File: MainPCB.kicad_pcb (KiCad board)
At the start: 4 copper layers, 105 x 62.4 mm, 42 parts, among them J1 RaspberryPi, J10 Conn_01x02, J12 Conn_01x07, J2 Conn_01x03, J3 Screw_Terminal_01x02, J4 Conn_01x02, J5 Conn_01x06, J6 Conn_01x03_Pin, J8 Conn_01x12, J9 Conn_01x04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

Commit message: Fixed Regulator Pins
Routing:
- net GND: track 398.8 -> 401.2 mm
- net 12V: track 240.5 -> 242.6 mm
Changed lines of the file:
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@@
 			)
 		)
+		(property ki_fp_filters "Connector*:*_1x??_*")
+		(sheetname "Root")
+		(sheetfile "MainPCB.kicad_sch")
 		(attr through_hole)
 		(fp_line
@@
 			(remove_unused_layers no)
 			(net 1 "GND")
-			(pinfunction "IN-")
+			(pinfunction "OUT-")
 			(pintype "input")
 		)
@@
 			)
 		)
+		(property ki_fp_filters "Connector*:*_1x??_*")
+		(sheetname "Root")
+		(sheetfile "MainPCB.kicad_sch")
 		(attr through_hole)
 		(fp_line
@@
 			)
 		)
-		(sheetname "Root")
-		(sheetfile "MainPCB.kicad_sch")
 		(attr through_hole)
 		(fp_rect
@@
 		)
 		(pad "1" thru_hole circle
-			(at 16.53 -1.27)
+			(at 6.37 -1.27)
 			(size 1.524 1.524)
 			(drill 0.762)
 			(layers "*.Cu" "*.Mask")
 			(remove_unused_layers no)
+			(pinfunction "OUT+")
+			(pintype "input")
 		)
 		(pad "3" thru_hole circle
-			(at 13.99 -1.27)
+			(at 8.91 -1.27)
 			(size 1.524 1.524)
 			(drill 0.762)
@@
 		)
 		(pad "4" thru_hole circle
-			(at 8.91 -1.27)
+			(at 11.45 -1.27)
 			(size 1.524 1.524)
 			(drill 0.762)
@@
 			(remove_unused_layers no)
 			(net 1 "GND")
-			(pinfunction "OUT-")
+			(pinfunction "IN-")
 			(pintype "input")
 		)
 		(pad "4" thru_hole circle
-			(at 11.45 -1.27)
+			(at 13.99 -1.27)
 			(size 1.524 1.524)
 			(drill 0.762)
@@
 			(remove_unused_layers no)
 			(net 1 "GND")
-			(pinfunction "OUT-")
+			(pinfunction "IN-")
 			(pintype "input")
 		)
 		(pad "5" thru_hole circle
-			(at 6.37 -1.27)
+			(at 16.53 -1.27)
 			(size 1.524 1.524)
 			(drill 0.762)
@@
 	)
 	(segment
-		(start 135.01 123.96)
-		(end 137.55 123.96)
-		(width 0.25)
+		(start 125.12 86.2)
+		(end 130.72 80.6)
+		(width 0.3)
 		(layer "F.Cu")
 		(net 1)
 	)
 	(segment
-		(start 125.12 86.2)
-		(end 130.72 80.6)
+		(start 137.55 123.96)
+		(end 140.09 123.96)
 		(width 0.3)
 		(layer "F.Cu")
@@
 	)
 	(segment
+		(start 120.6927 125.1439)
+		(end 113.9324 118.3836)
+		(width 0.3)
+		(layer "In1.Cu")
+		(net 1)
+	)
+	(segment
 		(start 177.8 120.2181)
 		(end 177.8 117.6)
@@
 	)
 	(segment
+		(start 136.3661 125.1439)
+		(end 120.6927 125.1439)
+		(width 0.3)
+		(layer "In1.Cu")
+		(net 1)
+	)
+	(segment
 		(start 162.8 81.3)
 		(end 166.9 85.4)
@@
 	)
 	(segment
+		(start 137.55 123.96)
+		(end 136.3661 125.1439)
+		(width 0.3)
+		(layer "In1.Cu")
+		(net 1)
+	)
+	(segment
 		(start 150.4261 97.0839)
 		(end 150.4261 111.3061)
@@
 	)
 	(segment
-		(start 134.0061 125.1439)
-		(end 120.6927 125.1439)
-		(width 0.3)
-		(layer "In1.Cu")
-		(net 1)
-	)
-	(segment
 		(start 137.578 79.3992)
 		(end 137.578 71.4128)
@@
 	)
 	(segment
-		(start 135.12 124.03)
-		(end 134.0061 125.1439)
-		(width 0.3)
-		(layer "In1.Cu")
-		(net 1)
-	)
-	(segment
 		(start 174.82 123.1981)
 		(end 177.8 120.2181)
@@
 	)
 	(segment
-		(start 120.6927 125.1439)
-		(end 113.9324 118.3836)
-		(width 0.3)
-		(layer "In1.Cu")
-		(net 1)
-	)
-	(segment
 		(start 113.27 111.2451)
 		(end 114.92 112.8951)
@@
 	)
 	(segment
-		(start 114.887968 109.14)
-		(end 114.54 109.14)
-		(width 1)
+		(start 146.03 120.56)
+		(end 151.307767 120.56)
+		(width 0.4)
 		(layer "F.Cu")
 		(net 3)
@@
 	)
 	(segment
-		(start 132.47 123.96)
-		(end 135.87 120.56)
-		(width 0.4)
+		(start 142.63 123.96)
+		(end 139.18 120.51)
+		(width 1)
 		(layer "F.Cu")
 		(net 3)
 	)
 	(segment
-		(start 157.15 112.91)
-		(end 158.4 111.66)
+		(start 157.15 114.717767)
+		(end 157.15 112.91)
 		(width 0.4)
 		(layer "F.Cu")
@@
 	)
 	(segment
-		(start 132.47 123.96)
-		(end 129.02 120.51)
+		(start 126.257968 120.51)
+		(end 114.887968 109.14)
+		(width 1)
+		(layer "F.Cu")
+		(net 3)
+	)
+	(segment
+		(start 114.887968 109.14)
+		(end 114.54 109.14)
 		(width 1)
 		(layer "F.Cu")
@@
 	)
 	(segment
-		(start 135.87 120.56)
-		(end 151.307767 120.56)
+		(start 157.15 112.91)
+		(end 158.4 111.66)
 		(width 0.4)
 		(layer "F.Cu")
@@
 	)
 	(segment
-		(start 157.15 114.717767)
-		(end 157.15 112.91)
+		(start 151.307767 120.56)
+		(end 157.15 114.717767)
 		(width 0.4)
 		(layer "F.Cu")
@@
 	)
 	(segment
-		(start 151.307767 120.56)
-		(end 157.15 114.717767)
+		(start 142.63 123.96)
+		(end 146.03 120.56)
 		(width 0.4)
 		(layer "F.Cu")
@@
 	)
 	(segment
-		(start 129.02 120.51)
+		(start 139.18 120.51)
 		(end 126.257968 120.51)
 		(width 1)
@@
 	)
 	(segment
-		(start 126.257968 120.51)
-		(end 114.887968 109.14)
-		(width 1)
-		(layer "F.Cu")
-		(net 3)
-	)
-	(segment
 		(start 89.56 86.2)
 		(end 95.84 92.48)
@@
 	)
 	(segment
-		(start 171.6592 109.5092)
-		(end 146.8384 109.5092)
+		(start 175.3 116.7303)
+		(end 174.05 115.4803)
 		(width 2)
 		(layer "In2.Cu")
@@
 	)
 	(segment
-		(start 146.8384 109.5092)
-		(end 140.09 116.2576)
+		(start 135.01 121.3376)
+		(end 135.01 123.96)
 		(width 2)
 		(layer "In2.Cu")
@@
 	)
 	(segment
-		(start 174.05 111.9)
-		(end 171.6592 109.5092)
+		(start 174.05 115.4803)
+		(end 174.05 111.9)
 		(width 2)
 		(layer "In2.Cu")
@@
 	)
 	(segment
-		(start 175.3 116.7303)
-		(end 174.05 115.4803)
+		(start 171.6592 109.5092)
+		(end 146.8384 109.5092)
 		(width 2)
 		(layer "In2.Cu")
@@
 	)
 	(segment
-		(start 175.3 117.6)
-		(end 175.3 116.7303)
+		(start 146.8384 109.5092)
+		(end 135.01 121.3376)
 		(width 2)
 		(layer "In2.Cu")
@@
 	)
 	(segment
-		(start 174.05 115.4803)
-		(end 174.05 111.9)
+		(start 175.3 117.6)
+		(end 175.3 116.7303)
 		(width 2)
 		(layer "In2.Cu")
@@
 	)
 	(segment
-		(start 140.09 116.2576)
-		(end 140.09 123.96)
+		(start 174.05 111.9)
+		(end 171.6592 109.5092)
 		(width 2)
 		(layer "In2.Cu")

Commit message: 3.3v thicken
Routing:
- net 3.3V: track 171.8 -> 204.7 mm
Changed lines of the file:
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@@
+	)
+	(segment
+		(start 117.08 106.6)
+		(end 118.9 106.6)
+		(width 0.75)
+		(layer "In2.Cu")
+		(net 6)
 	)
 	(segment
@@
 	)
 	(segment
-		(start 126.46 100.358929)
-		(end 133.418929 93.4)
-		(width 0.4)
+		(start 188.103 104.897)
+		(end 190.6 102.4)
+		(width 0.75)
 		(layer "In2.Cu")
 		(net 6)
 	)
 	(segment
-		(start 117.08 106.6)
-		(end 124.197057 106.6)
-		(width 0.4)
-		(layer "In2.Cu")
-		(net 6)
-	)
-	(segment
-		(start 124.197057 106.6)
-		(end 126.46 104.337057)
-		(width 0.4)
+		(start 120.603 104.897)
+		(end 188.103 104.897)
+		(width 0.75)
 		(layer "In2.Cu")
 		(net 6)
@@
 	)
 	(segment
-		(start 126.46 104.337057)
-		(end 126.46 100.358929)
-		(width 0.4)
+		(start 118.9 106.6)
+		(end 120.603 104.897)
+		(width 0.75)
 		(layer "In2.Cu")
 		(net 6)
-	)
-	(segment
-		(start 133.418929 93.4)
-		(end 151.57 93.4)
-		(width 0.4)
-		(layer "In2.Cu")
-		(net 6)

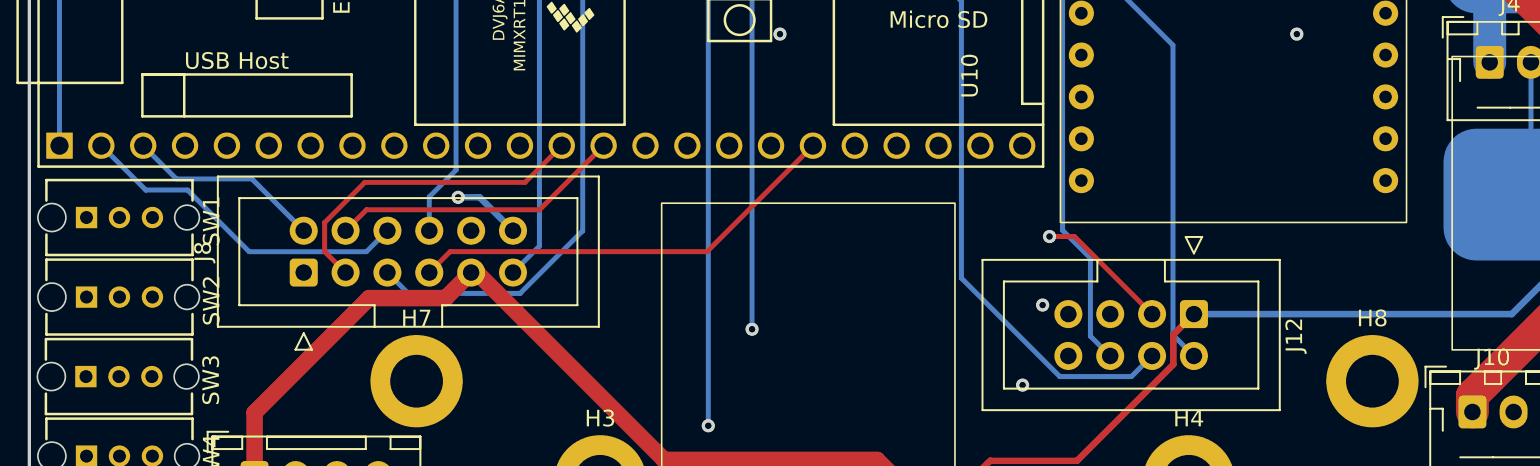
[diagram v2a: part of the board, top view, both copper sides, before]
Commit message: LED pulse to PWM
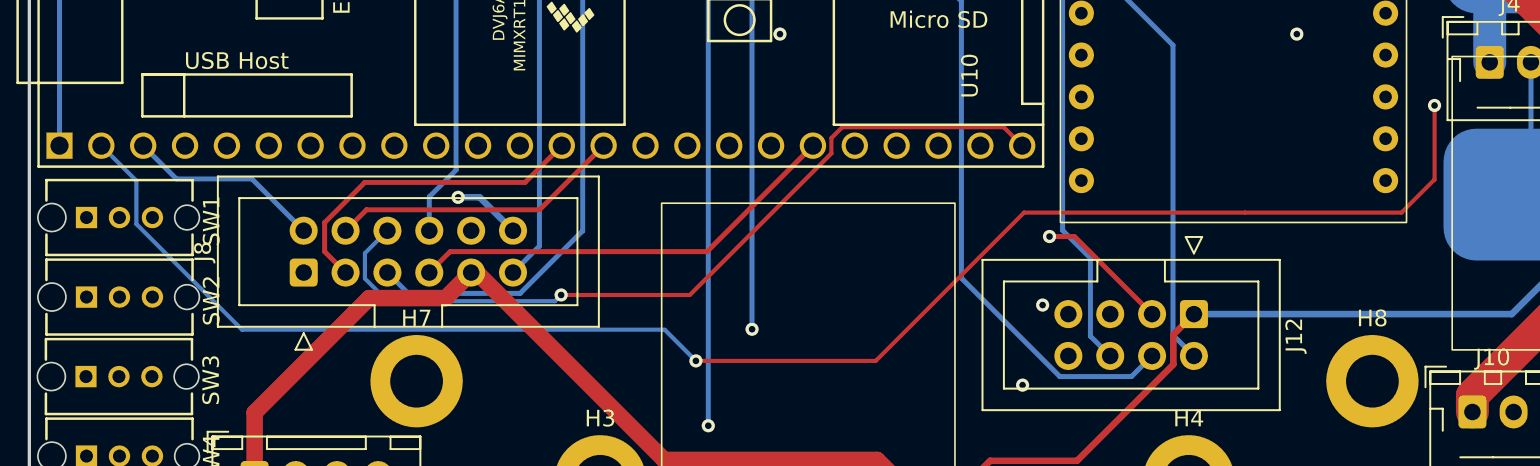
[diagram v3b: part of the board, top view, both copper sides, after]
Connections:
- U1 pad 2: CS1 -> LEDPulse
- U1 pad 24: LEDPulse -> CS1
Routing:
- net LEDPulse: track 40.0 -> 111.7 mm, vias 0 -> 2
- net CS1: track 20.5 -> 49.3 mm, vias 0 -> 1
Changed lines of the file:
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@@
 			(layers "*.Cu" "*.Mask")
 			(remove_unused_layers no)
-			(net 19 "CS1")
+			(net 35 "LEDPulse")
 			(pinfunction "0_RX1_CRX2_CS1")
 			(pintype "bidirectional")
@@
 			(layers "*.Cu" "*.Mask")
 			(remove_unused_layers no)
-			(net 35 "LEDPulse")
+			(net 19 "CS1")
 			(pinfunction "32_OUT1B")
 			(pintype "bidirectional")
@@
 			(remove_unused_layers no)
 			(net 1 "GND")
-			(pinfunction "OUT-")
+			(pinfunction "IN-")
 			(pintype "input")
 		)
@@
 			)
 		)
+		(sheetname "Root")
+		(sheetfile "MainPCB.kicad_sch")
 		(attr through_hole)
 		(fp_rect
@@
 			(layers "*.Cu" "*.Mask")
 			(remove_unused_layers no)
-			(pinfunction "OUT+")
-			(pintype "input")
 		)
 		(pad "3" thru_hole circle
@@
 	)
 	(segment
-		(start 97.3333 104.1333)
-		(end 101.07 107.87)
-		(width 0.3)
+		(start 147.98 101.44)
+		(end 146.855 100.315)
+		(width 0.25)
+		(layer "F.Cu")
+		(net 19)
+	)
+	(segment
+		(start 136.405 101.905991)
+		(end 127.810991 110.5)
+		(width 0.25)
+		(layer "F.Cu")
+		(net 19)
+	)
+	(segment
+		(start 137.064009 100.315)
+		(end 136.405 100.974009)
+		(width 0.25)
+		(layer "F.Cu")
+		(net 19)
+	)
+	(segment
+		(start 127.810991 110.5)
+		(end 120 110.5)
+		(width 0.25)
+		(layer "F.Cu")
+		(net 19)
+	)
+	(segment
+		(start 146.855 100.315)
+		(end 137.064009 100.315)
+		(width 0.25)
+		(layer "F.Cu")
+		(net 19)
+	)
+	(segment
+		(start 136.405 100.974009)
+		(end 136.405 101.905991)
+		(width 0.25)
+		(layer "F.Cu")
+		(net 19)
+	)
+	(via
+		(at 120 110.5)
+		(size 0.8)
+		(drill 0.4)
+		(layers "F.Cu" "B.Cu")
+		(net 19)
+	)
+	(segment
+		(start 119.6221 110.8779)
+		(end 109.4729 110.8779)
+		(width 0.25)
 		(layer "B.Cu")
 		(net 19)
 	)
 	(segment
-		(start 108.19 107.87)
+		(start 108.095 107.965)
 		(end 109.46 106.6)
-		(width 0.3)
+		(width 0.25)
 		(layer "B.Cu")
 		(net 19)
 	)
 	(segment
-		(start 92.1 101.44)
-		(end 94.7933 104.1333)
-		(width 0.3)
+		(start 109.4729 110.8779)
+		(end 108.095 109.5)
+		(width 0.25)
 		(layer "B.Cu")
 		(net 19)
 	)
 	(segment
-		(start 94.7933 104.1333)
-		(end 97.3333 104.1333)
-		(width 0.3)
+		(start 120 110.5)
+		(end 119.6221 110.8779)
+		(width 0.25)
 		(layer "B.Cu")
 		(net 19)
 	)
 	(segment
-		(start 101.07 107.87)
-		(end 108.19 107.87)
-		(width 0.3)
+		(start 108.095 109.5)
+		(end 108.095 107.965)
+		(width 0.25)
 		(layer "B.Cu")
 		(net 19)
@@
 	)
 	(segment
-		(start 149.67 99.75)
-		(end 161.6509 99.75)
-		(width 0.3)
-		(layer "In2.Cu")
+		(start 139.092749 114.5)
+		(end 148.092749 105.5)
+		(width 0.25)
+		(layer "F.Cu")
+		(net 35)
+	)
+	(segment
+		(start 171 105.5)
+		(end 173 103.5)
+		(width 0.25)
+		(layer "F.Cu")
 		(net 35)
 	)
 	(segment
-		(start 170.1209 91.28)
+		(start 128.18 114.5)
+		(end 139.092749 114.5)
+		(width 0.25)
+		(layer "F.Cu")
+		(net 35)
+	)
+	(segment
+		(start 148.092749 105.5)
+		(end 161.5 105.5)
+		(width 0.25)
+		(layer "F.Cu")
+		(net 35)
+	)
+	(segment
+		(start 161.5 105.5)
+		(end 171 105.5)
+		(width 0.25)
+		(layer "F.Cu")
+		(net 35)
+	)
+	(segment
+		(start 173 103.5)
+		(end 173 99)
+		(width 0.25)
+		(layer "F.Cu")
+		(net 35)
+	)
+	(via
+		(at 173 99)
+		(size 0.8)
+		(drill 0.4)
+		(layers "F.Cu" "B.Cu")
+		(net 35)
+	)
+	(via
+		(at 128.18 114.5)
+		(size 0.8)
+		(drill 0.4)
+		(layers "F.Cu" "B.Cu")
+		(net 35)
+	)
+	(segment
+		(start 179.2829 91.28)
 		(end 183.8 91.28)
-		(width 0.3)
+		(width 0.25)
 		(layer "In2.Cu")
 		(net 35)
 	)
 	(segment
-		(start 161.6509 99.75)
-		(end 170.1209 91.28)
-		(width 0.3)
+		(start 173 97.5629)
+		(end 179.2829 91.28)
+		(width 0.25)
 		(layer "In2.Cu")
 		(net 35)
 	)
 	(segment
-		(start 147.98 101.44)
-		(end 149.67 99.75)
-		(width 0.3)
+		(start 173 99)
+		(end 173 97.5629)
+		(width 0.25)
 		(layer "In2.Cu")
 		(net 35)
 	)
+	(segment
+		(start 94.227301 103.567301)
+		(end 94.227301 106.202906)
+		(width 0.25)
+		(layer "B.Cu")
+		(net 35)
+	)
+	(segment
+		(start 100.631295 112.6069)
+		(end 126.2869 112.6069)
+		(width 0.25)
+		(layer "B.Cu")
+		(net 35)
+	)
+	(segment
+		(start 94.227301 106.202906)
+		(end 100.631295 112.6069)
+		(width 0.25)
+		(layer "B.Cu")
+		(net 35)
+	)
+	(segment
+		(start 92.1 101.44)
+		(end 94.227301 103.567301)
+		(width 0.25)
+		(layer "B.Cu")
+		(net 35)
+	)
+	(segment
+		(start 126.2869 112.6069)
+		(end 128.18 114.5)
+		(width 0.25)
+		(layer "B.Cu")
+		(net 35)
+	)

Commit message: Changed Layout
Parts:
- removed J10: Conn_01x02, Connector_JST:JST_XH_B2B-XH-AM_1x02_P2.50mm_Vertical
- removed J12: Conn_01x07, Connector_IDC:IDC-Header_2x04_P2.54mm_Vertical
- removed J9: Conn_01x04, Connector_JST:JST_XH_B4B-XH-AM_1x04_P2.50mm_Vertical
- added C1: 10uf, Capacitor_SMD:C_0805_2012Metric, F.Cu at (104.6, 90.9)
- added C10: .1uf, Capacitor_SMD:C_0805_2012Metric, F.Cu at (130.1, 118.7)
- added C11: .1uf, Capacitor_SMD:C_0805_2012Metric, F.Cu at (178.2, 113.7)
- added C12: .1uf, Capacitor_SMD:C_0805_2012Metric, F.Cu at (178.2, 117.0)
- added C2: 10uf, Capacitor_SMD:C_0805_2012Metric, F.Cu at (104.6, 94.0)
- added C3: .1uf, Capacitor_SMD:C_0805_2012Metric, F.Cu at (130.2, 105.6)
- added C4: .1uf, Capacitor_SMD:C_0805_2012Metric, F.Cu at (130.3, 108.2)
- added C5: .1uf, Capacitor_SMD:C_0805_2012Metric, F.Cu at (175.0, 90.3)
- added C6: .1uf, Capacitor_SMD:C_0805_2012Metric, F.Cu at (175.0, 93.7)
- added C7: .1uf, Capacitor_SMD:C_0805_2012Metric, F.Cu at (105.4, 109.2)
- added C8: .1uf, Capacitor_SMD:C_0805_2012Metric, F.Cu at (105.4, 112.5)
- added C9: .1uf, Capacitor_SMD:C_0805_2012Metric, F.Cu at (130.1, 115.3)
- added J7: Conn_01x05, Connector_JST:JST_XH_B5B-XH-A_1x05_P2.50mm_Vertical, F.Cu at (100.3, 67.4)
- added M5: Motor_DC, Connector_JST:JST_XH_B2B-XH-AM_1x02_P2.50mm_Vertical, B.Cu at (163.4, 79.4)
- added R6: 15k, Capacitor_SMD:C_0805_2012Metric, F.Cu at (98.5, 82.4)
- added R7: 10k, Capacitor_SMD:C_0805_2012Metric, F.Cu at (101.5, 82.4)
- added U7: V_Regulator5v, Custom:Pololu Regulator, F.Cu at (123.8, 118.9)
- added U8: VNH Driver, MotorDriver:VNHDriver, F.Cu at (162.2, 76.5)
- J2: value Conn_01x03 -> Conn_01x05; footprint Connector_JST:JST_XH_B3B-XH-AM_1x03_P2.50mm_Vertical -> Connector_JST:JST_XH_B5B-XH-A_1x05_P2.50mm_Vertical
- J3: footprint SMDPads:Pads_1x02_XL -> Connector_AMASS:AMASS_XT60-F_1x02_P7.20mm_Vertical; moved to F.Cu
- J4: footprint Connector_JST:JST_XH_B2B-XH-AM_1x02_P2.50mm_Vertical -> Connector_PinHeader_2.54mm:PinHeader_2x01_P2.54mm_Vertical
- J8, M4: moved to B.Cu
- U11: footprint Custom:Pololu Regulator -> Custom:Pololu5V3.4A
- moved R1 84.2 mm to (99.6, 93.2), turned to 180 degrees
- moved J5 78.6 mm to (101.5, 118.3), turned to 180 degrees
- moved D1 72.9 mm to (94.0, 84.2)
- moved M3 63.2 mm to (185.4, 86.7), turned to 0 degrees
- moved U4 60.0 mm to (183.9, 73.3), turned to 90 degrees
- moved U5 55.4 mm to (128.3, 76.0), turned to 90 degrees
- moved U13 50.0 mm to (144.8, 72.7), turned to -90 degrees
- moved J6 49.5 mm to (106.5, 121.7), turned to 0 degrees
- moved M4 47.4 mm to (123.2, 76.0)
- moved U3 44.7 mm to (140.7, 114.3), turned to -90 degrees
- moved U11 44.4 mm to (165.4, 104.6), turned to 180 degrees
- moved J8 43.5 mm to (147.3, 115.8)
- moved U6 31.8 mm to (189.2, 92.5)
- moved M1 30.0 mm to (114.8, 81.8), turned to 0 degrees
- moved U2 29.6 mm to (112.6, 70.1)
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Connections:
- J1 pad 1: 5V -> Net-(J1-Pin_1)
- J2 pad 1: GND -> Net-(J2-Pin_1)
- J2 pad 2: 3.3V -> GND
- J2 pad 3: ESC -> TRIG1
- J5 pad 2: 3.3V -> Net-(J5-Pin_2)
- J8 pad 12: 3.3V -> Net-(J8-Pin_12)
- U1 pad 38: RX4->TX -> unconnected-(U1-16_A2_RX4_SCL1-Pad38)
- U1 pad 39: TX4->RX -> STATE
- U1 pad 48: 5V -> Net-(U1-VIN)
- U1 pad 8: ESC -> PWM5
- U10 pad 1: 3.3V -> Net-(U10-3.3v)
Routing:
- net GND: track 401.2 -> 0.00 mm, vias 1 -> 0
- net 12V: track 242.6 -> 0.00 mm
- net 3.3V: track 204.7 -> 0.00 mm, vias 1 -> 0
- net 5V: track 169.8 -> 0.00 mm
- net LEDPulse: track 111.7 -> 0.00 mm, vias 2 -> 0
- net Net-(J3-Pin_2): track 97.9 -> 0.00 mm
- net SLIDE4: track 94.4 -> 0.00 mm, vias 1 -> 0
- net DIR4A: track 92.9 -> 0.00 mm, vias 2 -> 0
- net SLIDE1: track 90.1 -> 0.00 mm, vias 2 -> 0
- net PWM4: track 88.1 -> 0.00 mm, vias 2 -> 0
- net ESC: track 84.6 -> 0.00 mm
- net SLIDE3: track 80.1 -> 0.00 mm, vias 1 -> 0
- net TX4->RX: track 79.1 -> 0.00 mm, vias 1 -> 0
- net SLIDE2: track 77.5 -> 0.00 mm, vias 1 -> 0
- net RX4->TX: track 75.7 -> 0.00 mm, vias 1 -> 0
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
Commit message: routing
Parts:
- C1, C11, C12, C2, C7, C8, R2, R3, R4, R5, R6, R7: moved to B.Cu
- moved J3 17.5 mm to (177.0, 112.7)
- moved C11 16.5 mm to (183.5, 98.0), turned to 0 degrees
- moved C12 16.5 mm to (183.5, 101.3), turned to 0 degrees
- moved J2 13.8 mm to (189.5, 99.2), turned to -90 degrees
- moved R2 9.03 mm to (137.6, 92.1)
- moved R5 9.03 mm to (146.6, 92.1)
- moved C8 3.53 mm to (105.4, 109.0)
- moved C7 3.17 mm to (105.4, 112.3)
- moved R3 3.01 mm to (140.6, 92.1)
- moved R4 3.01 mm to (143.6, 92.1)
- moved R6 3.01 mm to (101.5, 82.4)
- moved R7 3.01 mm to (98.5, 82.4)
- moved M4 2.40 mm to (123.9, 73.7)
- moved J7 1.57 mm to (99.8, 65.9)
- moved C9 1.07 mm to (129.0, 115.2)
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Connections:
- C1 pad 1: Net-(U1-VIN) -> 5V
- C10 pad 1: Net-(J8-Pin_12) -> 3.3V
- C11 pad 1: Net-(J2-Pin_1) -> 3.3V
- C12 pad 1: Net-(J2-Pin_1) -> 3.3V
- C2 pad 1: Net-(U1-VIN) -> 5V
- C3 pad 1: Net-(J1-Pin_1) -> 5V
- C4 pad 1: Net-(J1-Pin_1) -> 5V
- C5 pad 1: Net-(U10-3.3v) -> 3.3V
- C6 pad 1: Net-(U10-3.3v) -> 3.3V
- C7 pad 1: Net-(J5-Pin_2) -> 5V
- C8 pad 1: Net-(J5-Pin_2) -> 5V
- C9 pad 1: Net-(J8-Pin_12) -> 3.3V
- J1 pad 1: Net-(J1-Pin_1) -> 5V
- J2 pad 1: Net-(J2-Pin_1) -> 3.3V
- J5 pad 2: Net-(J5-Pin_2) -> 5V
- J7 pad 1: Net-(J2-Pin_1) -> 3.3V
- J8 pad 12: Net-(J8-Pin_12) -> 3.3V
- U1 pad 48: Net-(U1-VIN) -> 5V
- U10 pad 1: Net-(U10-3.3v) -> 3.3V
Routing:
- net 12V: track 0.00 -> 221.5 mm
- net Net-(J3-Pin_2): track 0.00 -> 162.3 mm
- net 5V: track 0.00 -> 133.9 mm
- net 3.3V: track 0.00 -> 104.6 mm, vias 0 -> 1

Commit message: moved stuff
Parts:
- J6: moved to B.Cu
- U6: moved to F.Cu
- moved U6 41.7 mm to (157.2, 65.8), turned to 0 degrees
- moved J4 21.3 mm to (169.7, 108.7), turned to 90 degrees
- moved J6 20.5 mm to (121.2, 106.9)
- moved J1 16.2 mm to (101.7, 105.9)
- moved C8 12.1 mm to (107.5, 120.9)
- moved C7 12.1 mm to (107.5, 124.2)
- moved J5 6.48 mm to (103.6, 124.0), turned to -90 degrees
- moved M3 2.71 mm to (185.4, 84.0)
- moved J2 2.45 mm to (189.5, 96.8)
- moved U4 1.65 mm to (183.9, 71.6)
- moved M4 1.37 mm to (124.5, 75.0)
- moved D1 1.37 mm to (93.5, 83.3)
- moved J7 1.19 mm to (100.8, 65.3)
- moved M1 1.08 mm to (115.9, 82.0)
- moved J3 1.02 mm to (177.0, 113.7)
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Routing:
- net 5V: track 133.9 -> 96.9 mm
- net Net-(J3-Pin_2): track 162.3 -> 147.7 mm
- net 12V: track 221.5 -> 228.8 mm
- net 3.3V: track 104.6 -> 109.3 mm

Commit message: moved stuff
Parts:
- moved J7 17.8 mm to (118.6, 66.1)
- moved R6 17.6 mm to (97.3, 65.3), turned to 180 degrees
- moved R7 14.1 mm to (97.3, 68.3), turned to 180 degrees
- moved U2 9.80 mm to (105.4, 76.5), turned to 0 degrees
- moved M4 1.63 mm to (125.0, 73.4)
- moved M1 1.05 mm to (116.9, 82.3)
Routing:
- net Net-(J3-Pin_2): track 147.7 -> 159.0 mm

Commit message: moved more stuff
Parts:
- moved J5 13.0 mm to (99.8, 111.5), turned to 0 degrees
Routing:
- net 3.3V: track 109.3 -> 0.00 mm, vias 1 -> 0
- net 5V: track 96.9 -> 23.1 mm
- net Net-(J3-Pin_2): track 159.0 -> 156.8 mm
